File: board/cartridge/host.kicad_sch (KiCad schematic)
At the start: 13 parts, among them P1 Card Edge, U4 TXS0108E, U5 74LVC245, U6 74LVC1G17, U7 74LVC245, U8 74LVC245, U9 PCM5100

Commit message: Remove watch crystal and audio DAC.
These can be implemented later; they're not needed
for a first-gen prototype to determine whether the
ESP32-S3 will even be able to bit-bang the bus.
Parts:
- removed U9: PCM5100, Package_SO:TSSOP-20_4.4x6.5mm_P0.65mm, symbol Audio:PCM5100
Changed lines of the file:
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@@
 	(wire
 		(pts
-			(xy 194.31 64.77) (xy 196.85 64.77)
-		)
-		(stroke
-			(width 0)
-			(type default)
-		)
-	)
-	(wire
-		(pts
 			(xy 91.44 143.51) (xy 96.52 143.51)
 		)
@@
 		)
 	)
-	(wire
-		(pts
-			(xy 194.31 67.31) (xy 196.85 67.31)
-		)
-		(stroke
-			(width 0)
-			(type default)
-		)
-	)
 	(bus
 		(pts
@@
 	(wire
 		(pts
-			(xy 194.31 69.85) (xy 196.85 69.85)
-		)
-		(stroke
-			(width 0)
-			(type default)
-		)
-	)
-	(wire
-		(pts
 			(xy 228.6 143.51) (xy 233.68 143.51)
 		)
@@
 		)
 	)
-	(hierarchical_label "I2S_DIN"
-		(shape input)
-		(at 194.31 67.31 180)
-		(fields_autoplaced yes)
-		(effects
-			(font
-				(size 1.27 1.27)
-			)
-			(justify right)
-		)
-	)
 	(hierarchical_label "~{HALT}"
 		(shape bidirectional)
@@
 		)
 	)
-	(hierarchical_label "I2S_LRCK"
-		(shape input)
-		(at 194.31 64.77 180)
-		(fields_autoplaced yes)
-		(effects
-			(font
-				(size 1.27 1.27)
-			)
-			(justify right)
-		)
-	)
 	(hierarchical_label "H[0..7]"
 		(shape tri_state)
@@
 		)
 	)
-	(hierarchical_label "I2S_BCK"
-		(shape input)
-		(at 194.31 69.85 180)
-		(fields_autoplaced yes)
-		(effects
-			(font
-				(size 1.27 1.27)
-			)
-			(justify right)
-		)
-	)
 	(hierarchical_label "~{SLENB}"
 		(shape bidirectional)
@@
 					(unit 1)
 				)
-			)
-		)
-	)
-	(symbol
-		(lib_id "Audio:PCM5100")
-		(at 209.55 74.93 0)
-		(unit 1)
-		(exclude_from_sim no)
-		(in_bom yes)
-		(on_board yes)
-		(dnp no)
-		(fields_autoplaced yes)
-		(property "Reference" "U9"
-			(at 214.2841 57.15 0)
-			(effects
-				(font
-					(size 1.27 1.27)
-				)
-				(justify left)
-			)
-		)
-		(property "Value" "PCM5100"
-			(at 214.2841 59.69 0)
-			(effects
-				(font
-					(size 1.27 1.27)
-				)
-				(justify left)
-			)
-		)
-		(property "Footprint" "Package_SO:TSSOP-20_4.4x6.5mm_P0.65mm"
-			(at 208.28 55.88 0)
-			(effects
-				(font
-					(size 1.27 1.27)
-				)
-				(hide yes)
-			)
-		)
-		(property "Datasheet" "http://www.ti.com/lit/ds/symlink/pcm5100.pdf"
-			(at 208.28 55.88 0)
-			(effects
-				(font
-					(size 1.27 1.27)
-				)
-				(hide yes)
-			)
-		)
-		(property "Description" "2VRMS DirectPath, 100dB Audio Stereo DAC with 32-bit, 384kHz PCM Interface, TSSOP-20"
-			(at 209.55 74.93 0)
-			(effects
-				(font
-					(size 1.27 1.27)
-				)
-				(hide yes)
-			)
-		)
-		(pin "16"
-		)
-		(pin "1"
-		)
-		(pin "4"
-		)
-		(pin "13"
-		)
-		(pin "20"
-		)
-		(pin "14"
-		)
-		(pin "11"
-		)
-		(pin "10"
-		)
-		(pin "15"
-		)
-		(pin "12"
-		)
-		(pin "6"
-		)
-		(pin "3"
-		)
-		(pin "8"
-		)
-		(pin "2"
-		)
-		(pin "18"
-		)
-		(pin "5"
-		)
-		(pin "7"
-		)
-		(pin "19"
-		)
-		(pin "17"
-		)
-		(pin "9"
-		)
-		(instances
-			(project "cartridge"
-				(path "/b6472d2e-e93c-4ee2-a887-2e70fff347c6/c8484109-b338-40e2-9818-5e104bae91b8"
-					(reference "U9")
-					(unit 1)
-				)

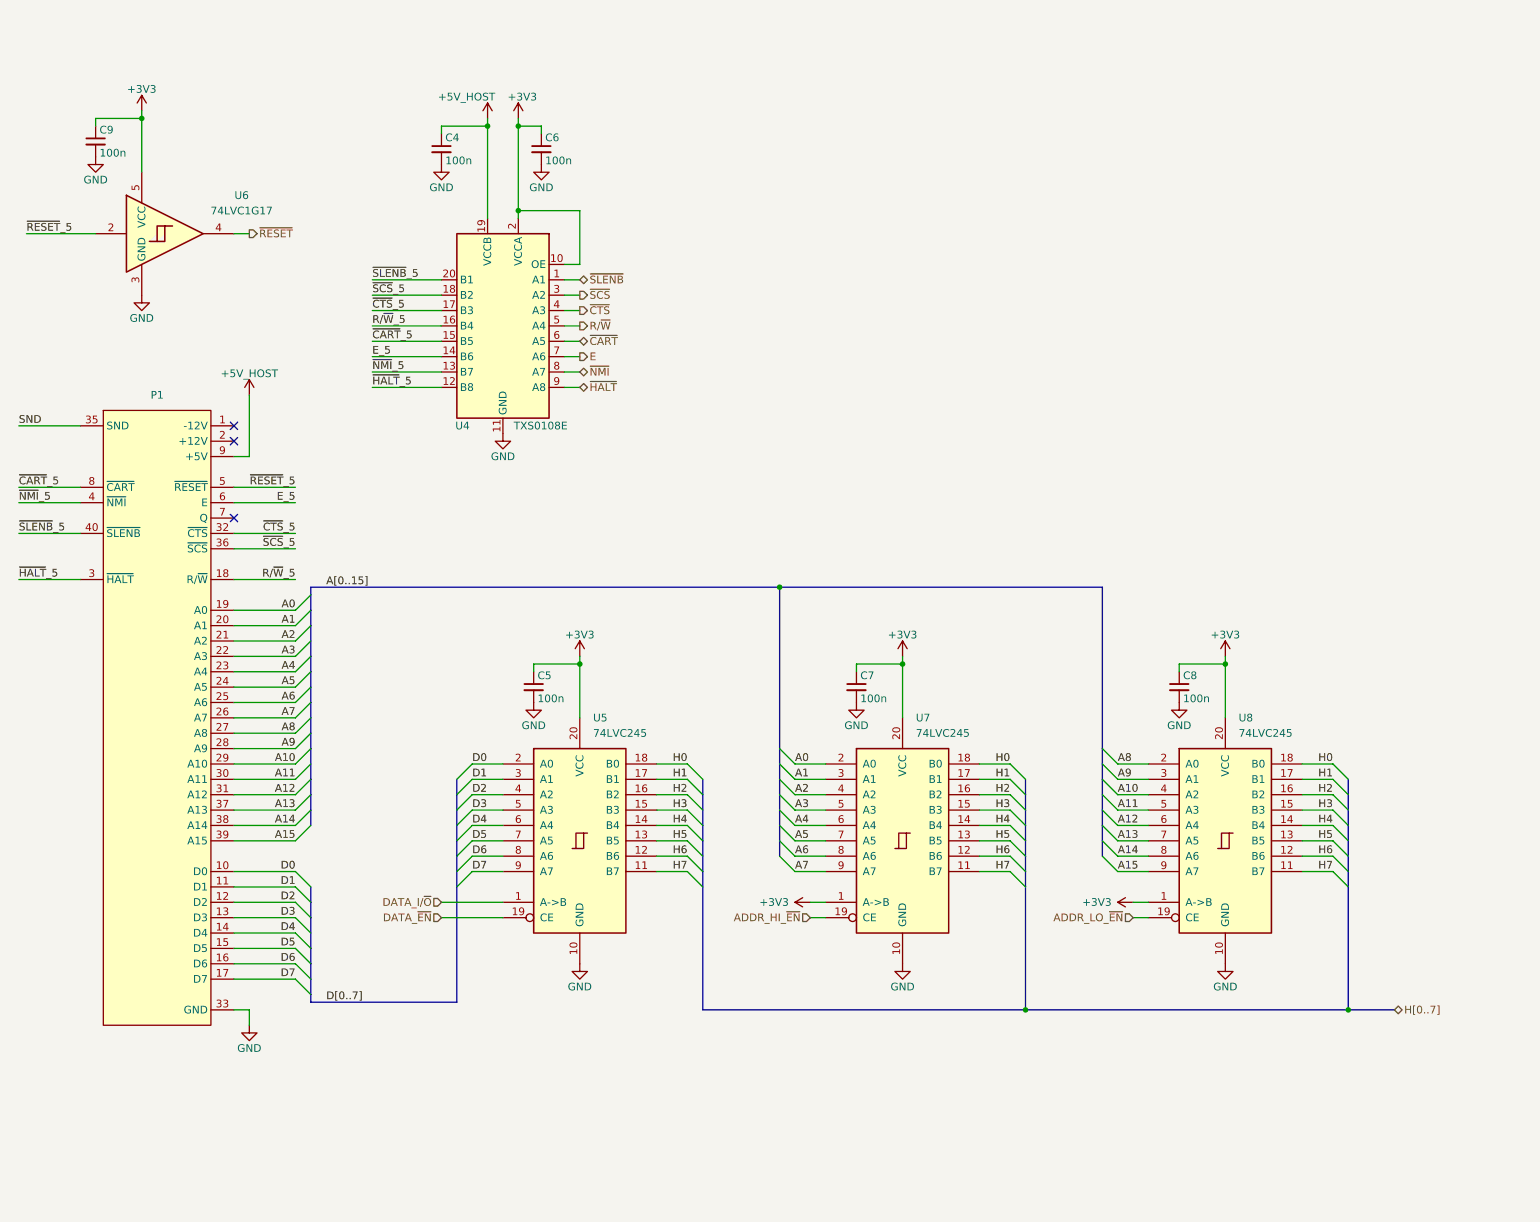
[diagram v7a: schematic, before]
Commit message: Start adjusting select logic for testing.
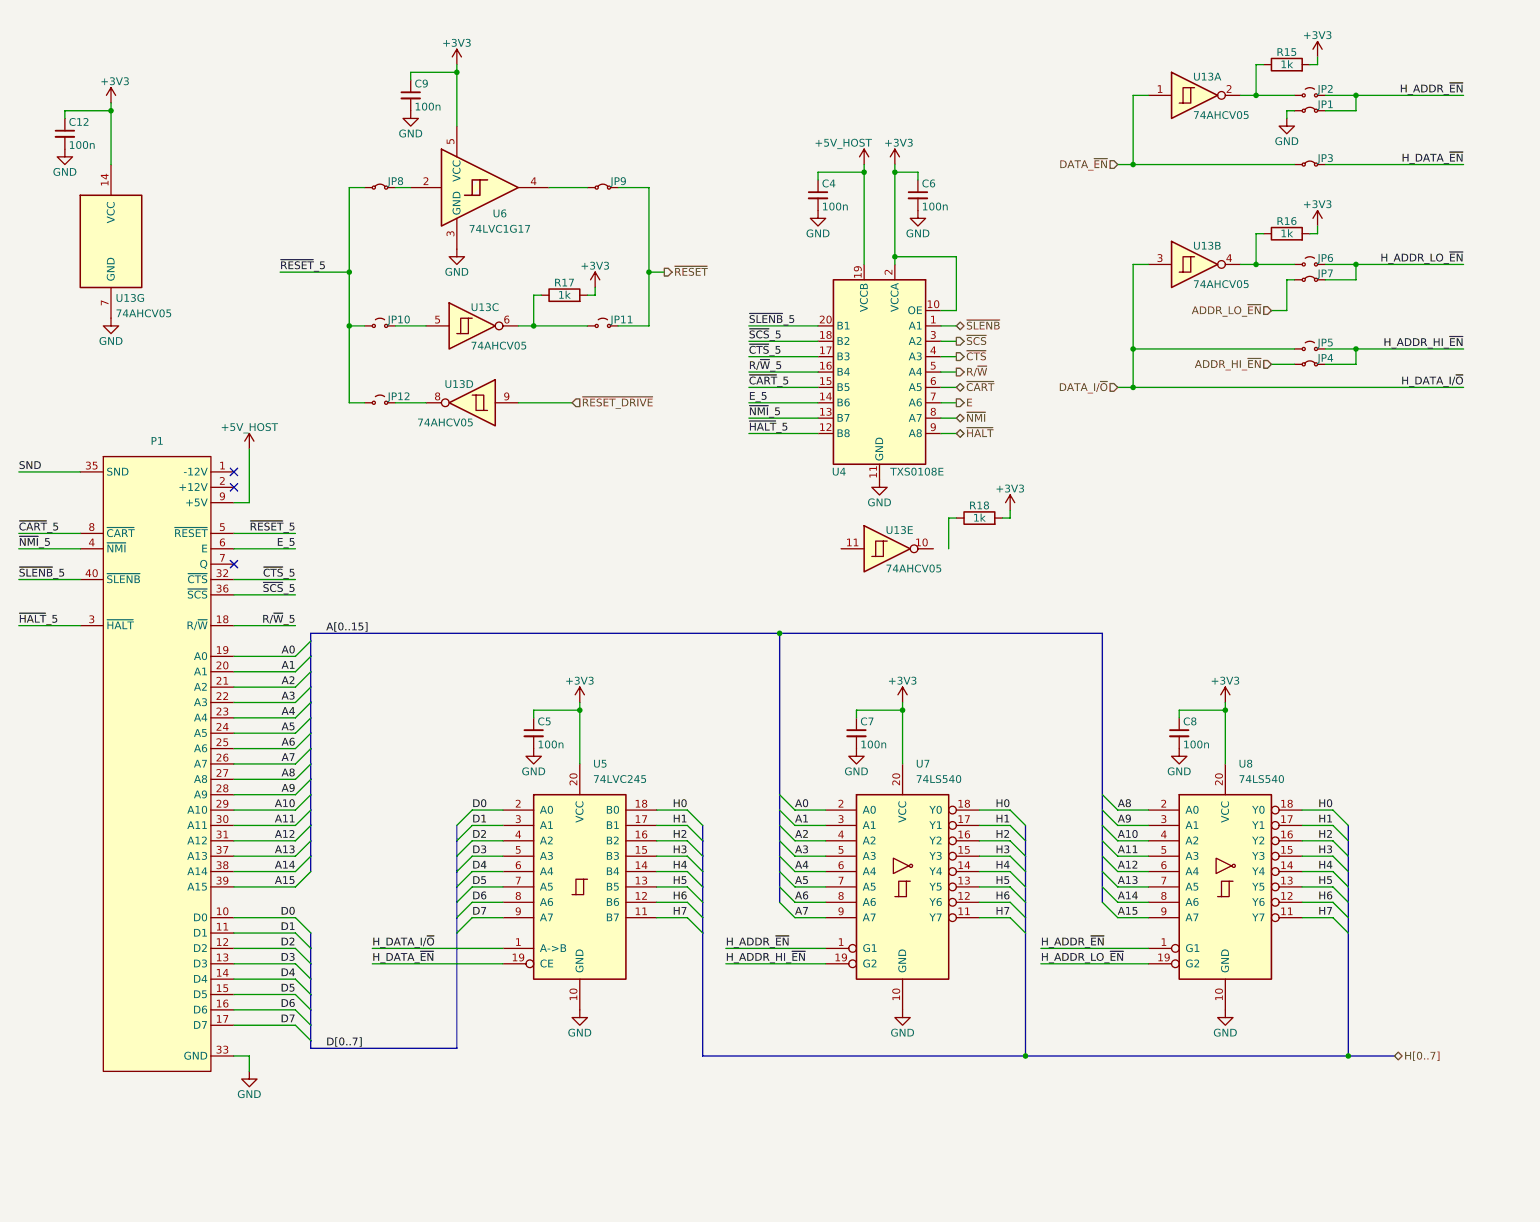
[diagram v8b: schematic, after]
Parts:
- removed U7, U8: 74LVC245, Package_SO:TSSOP-20_4.4x6.5mm_P0.65mm, symbol 74xx:74LS245
- added C12: 100n, Capacitor_SMD:C_0603_1608Metric, symbol Device:C_Small
- added JP1, JP3, JP4, JP7, JP8, JP9: Jumper_2_Small_Bridged, Jumper:SolderJumper-2_P1.3mm_Open_TrianglePad1.0x1.5mm, symbol Jumper:Jumper_2_Small_Bridged
- added JP10, JP11, JP12, JP2, JP5, JP6: Jumper_2_Small_Open, Jumper:SolderJumper-2_P1.3mm_Open_TrianglePad1.0x1.5mm, symbol Jumper:Jumper_2_Small_Open
- added R15, R16, R17, R18: 1k, Resistor_SMD:R_0603_1608Metric, symbol Device:R
- added U13: 74AHCV05, Package_SO:TSSOP-14_4.4x5mm_P0.65mm, symbol 74xx:74LS14
- added U7, U8: 74LS540, symbol 74xx:74LS540
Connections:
- net +3V3: now also C12.1, R15.2, R16.2, R17.2, R18.2, U13.14 (VCC), U7.20 (VCC), U8.20 (VCC)
- net A0: now also U7.2 (A0)
- net A1: now also U7.3 (A1)
- net A10: now also U8.4 (A2)
- net A11: now also U8.5 (A3)
- net A12: now also U8.6 (A4)
- net A13: now also U8.7 (A5)
- net A14: now also U8.8 (A6)
- net A15: now also U8.9 (A7)
- net A2: now also U7.4 (A2)
- net A3: now also U7.5 (A3)
- net A4: now also U7.6 (A4)
- net A5: now also U7.7 (A5)
- net A6: now also U7.8 (A6)
- net A7: now also U7.9 (A7)
- net A8: now also U8.2 (A0)
- net A9: now also U8.3 (A1)
- net ADDR_HI_~{EN}: now also JP4.1 (A)
- net ADDR_LO_~{EN}: now also JP7.1 (A)
- net DATA_I/~{O}: now also JP5.1 (A), U13.3
- net DATA_~{EN}: now also JP3.1 (A), U13.1; no longer U5.19 (CE)
- net GND: now also C12.2, JP1.1 (A), U13.7 (GND), U7.10 (GND), U8.10 (GND)
- net H0: now also U7.18 (Y0), U8.18 (Y0)
- net H1: now also U7.17 (Y1), U8.17 (Y1)
- net H2: now also U7.16 (Y2), U8.16 (Y2)
- net H3: now also U7.15 (Y3), U8.15 (Y3)
- net H4: now also U7.14 (Y4), U8.14 (Y4)
- net H5: now also U7.13 (Y5), U8.13 (Y5)
- net H6: now also U7.12 (Y6), U8.12 (Y6)
- net H7: now also U7.11 (Y7), U8.11 (Y7)
- net ~{RESET}: now also JP11.2 (B), JP9.2 (B); no longer U6.4
- net ~{RESET}_5: now also JP10.1 (A), JP12.1 (A), JP8.1 (A); no longer U6.2
- new net: JP12.2 (B), U13.8
- new net: JP2.1 (A), R15.1, U13.2
- new net: JP10.2 (B), U13.5
- new net: JP6.1 (A), R16.1, U13.4
- new net: JP11.1 (A), R17.1, U13.6
- new net: JP9.1 (A), U6.4
- new net: JP8.2 (B), U6.2
- new net H_ADDR_HI_~{EN}: JP4.2 (B), JP5.2 (B), U7.19 (G2)
- new net H_ADDR_LO_~{EN}: JP6.2 (B), JP7.2 (B), U8.19 (G2)
- new net H_ADDR_~{EN}: JP1.2 (B), JP2.2 (B), U7.1 (G1), U8.1 (G1)
- new net H_DATA_~{EN}: JP3.2 (B), U5.19 (CE)
- new net ~{RESET_DRIVE}: U13.9
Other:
- moved on the sheet: C4, C5, C6, C7, C8, C9, P1, U4, U5, U6
